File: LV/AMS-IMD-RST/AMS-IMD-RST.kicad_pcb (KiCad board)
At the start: 2 copper layers, 66.8 x 64.2 mm, 38 parts, among them J1 2P Droit 2-11-2022, J2 2P Droit 2-11-2022, J3 2P Droit 2-11-2022, J4 2P Droit 2-11-2022, J5 2P Droit 2-11-2022, J6 2P Droit 2-11-2022, J7 4P Droit 22-11-2042, K1 Relais PCB, K3 Relais PCB, Q5 NMOS SQ2348ES-T1_GE3, Q6 NMOS SQ2348ES-T1_GE3, U1 Alim LP TSR_0.5-2450, U10 TLV172IDCK, U11 74AUC2G00, U14 74AHC1G08, U15 74AHC1G08, U16 74AHC1G08, U17 TLV172IDCK, U2 MCP6562, U3 74AHC1G32, U4 74AUC2G04, U5 MCP6562, U6 MCP6562, U7 74LS279, U9 TLV172IDCK

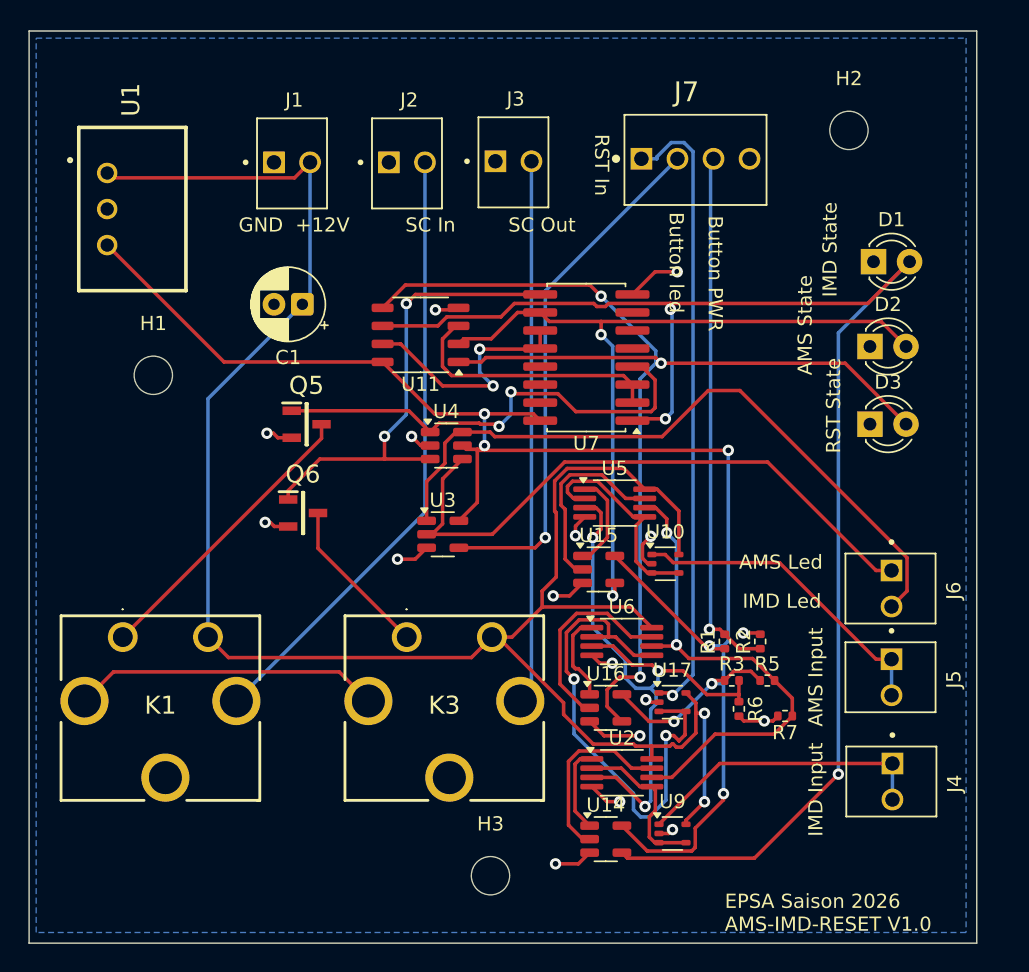
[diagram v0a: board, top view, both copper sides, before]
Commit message: Added 2s lightning for T11.9.6 compliance
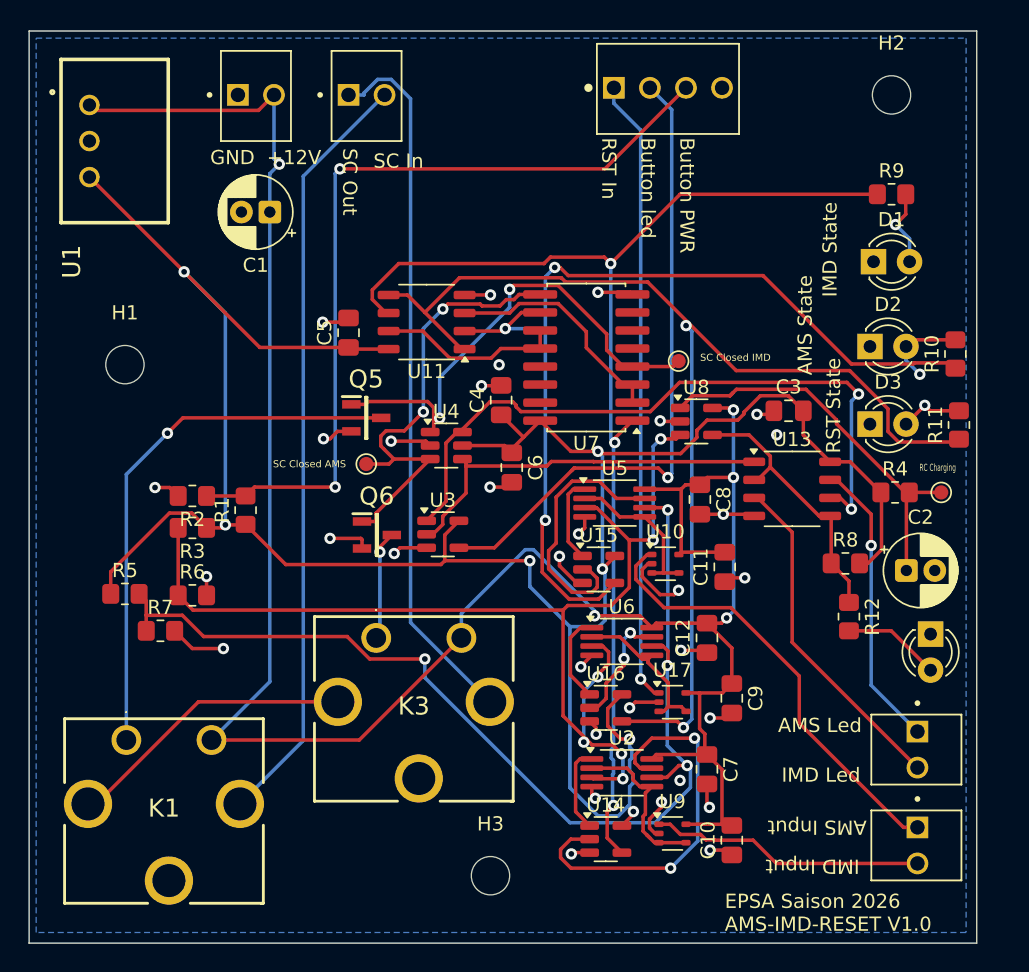
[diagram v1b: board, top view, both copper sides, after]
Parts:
- removed J3, J5: 2P Droit 2-11-2022, EPSA_lib:MOLEX_22-11-2022
- added C10: 100n, Capacitor_SMD:C_0805_2012Metric_Pad1.18x1.45mm_HandSolder, F.Cu at (117.8, 92.8)
- added C11: 100n, Capacitor_SMD:C_0805_2012Metric_Pad1.18x1.45mm_HandSolder, F.Cu at (117.2, 73.5)
- added C12: 100n, Capacitor_SMD:C_0805_2012Metric_Pad1.18x1.45mm_HandSolder, F.Cu at (116.0, 78.5)
- added C2: 10u, Capacitor_THT:CP_Radial_D5.0mm_P2.00mm, F.Cu at (130.0, 73.8)
- added C3: 100n, Capacitor_SMD:C_0805_2012Metric_Pad1.18x1.45mm_HandSolder, F.Cu at (121.8, 62.5)
- added C4: 100n, Capacitor_SMD:C_0805_2012Metric_Pad1.18x1.45mm_HandSolder, F.Cu at (101.5, 61.8)
- added C5: 100n, Capacitor_SMD:C_0805_2012Metric_Pad1.18x1.45mm_HandSolder, F.Cu at (90.8, 57.0)
- added C6: 100n, Capacitor_SMD:C_0805_2012Metric_Pad1.18x1.45mm_HandSolder, F.Cu at (102.2, 66.5)
- added C7: 100n, Capacitor_SMD:C_0805_2012Metric_Pad1.18x1.45mm_HandSolder, F.Cu at (116.0, 87.8)
- added C8: 100n, Capacitor_SMD:C_0805_2012Metric_Pad1.18x1.45mm_HandSolder, F.Cu at (115.5, 68.8)
- added C9: 100n, Capacitor_SMD:C_0805_2012Metric_Pad1.18x1.45mm_HandSolder, F.Cu at (117.8, 82.8)
- added D4: LED, LED_THT:LED_D3.0mm, F.Cu at (131.8, 78.2)
- added R10: 10k, Resistor_SMD:R_0805_2012Metric_Pad1.20x1.40mm_HandSolder, F.Cu at (133.5, 58.5)
- added R11: 10k, Resistor_SMD:R_0805_2012Metric_Pad1.20x1.40mm_HandSolder, F.Cu at (133.8, 63.5)
- added R12: 10k, Resistor_SMD:R_0805_2012Metric_Pad1.20x1.40mm_HandSolder, F.Cu at (126.0, 77.0)
- added R4: 62k, Resistor_SMD:R_0805_2012Metric_Pad1.20x1.40mm_HandSolder, F.Cu at (129.2, 68.2)
- added R8: 10k, Resistor_SMD:R_0805_2012Metric_Pad1.20x1.40mm_HandSolder, F.Cu at (125.8, 73.2)
- added R9: 10k, Resistor_SMD:R_0805_2012Metric_Pad1.20x1.40mm_HandSolder, F.Cu at (129.0, 47.2)
- added TP1: type="R" model="TestPoint" lib="", TestPoint:TestPoint_Pad_D1.0mm, F.Cu at (92.0, 66.2)
- added TP2: type="R" model="TestPoint" lib="", TestPoint:TestPoint_Pad_D1.0mm, F.Cu at (114.0, 59.0)
- added TP3: type="R" model="TestPoint" lib="", TestPoint:TestPoint_Pad_D1.0mm, F.Cu at (132.5, 68.2)
- added U13: 74AUC2G32, Package_SO:SSOP-8_3.9x5.05mm_P1.27mm, F.Cu at (122.0, 68.0)
- added U8: LM397, Package_TO_SOT_SMD:SOT-23-5, F.Cu at (115.2, 63.2)
- R1, R2, R3, R5, R6, R7: footprint Resistor_SMD:R_0402_1005Metric -> Resistor_SMD:R_0805_2012Metric_Pad1.20x1.40mm_HandSolder
- moved R5 45.7 mm to (75.0, 75.4)
- moved R7 44.4 mm to (77.5, 78.0), turned to 0 degrees
- moved R2 41.3 mm to (79.8, 68.5), turned to 180 degrees
- moved R3 39.5 mm to (79.8, 70.8), turned to 180 degrees
- moved R6 39.3 mm to (79.8, 75.5), turned to 0 degrees
- moved R1 35.0 mm to (83.5, 69.5)
- moved J6 11.5 mm to (130.8, 85.1)
- moved K1 7.25 mm to (75.1, 85.7)
- moved C1 6.89 mm to (85.2, 48.5)
- moved J2 5.54 mm to (90.8, 40.2)
- moved Q6 5.43 mm to (92.8, 71.2)
- moved J1 5.39 mm to (83.0, 40.2)
- moved J7 5.36 mm to (113.2, 39.8)
- moved U1 4.95 mm to (70.5, 37.8)
- moved J4 4.83 mm to (130.8, 91.8)
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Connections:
- D1 pad 2: /IMD_State -> Net-(D1-A)
- D2 pad 2: /AMS_State -> Net-(D2-A)
- D3 pad 2: /Button_Output_State -> Net-(D3-A)
- J2 pad 1: GND -> /SC out
- J4 pad 1: /Raw_IMD_OK -> /Raw_AMS_OK
- U3 pad 1: /IMD_Led -> /Raw_IMD_Led
- U3 pad 2: /AMS_Led -> /Raw_AMS_Led
- U4 pad 4: /AMS_Led -> /Raw_AMS_Led
- U4 pad 6: /IMD_Led -> /Raw_IMD_Led
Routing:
- net +5V: track 122.4 -> 178.7 mm
- net /Raw_IMD_Led: track 0.00 -> 48.1 mm, vias 0 -> 2
- net /3.5V: track 35.5 -> 76.1 mm, vias 2 -> 4
- net /4V: track 44.3 -> 81.0 mm, vias 3 -> 6
- net Net-(U8--): track 0.00 -> 27.9 mm
- net /Raw_AMS_Led: track 0.00 -> 27.3 mm
- net Net-(U17--): track 36.4 -> 11.1 mm, vias 2 -> 0
- net /IMD_Led: track 49.1 -> 23.9 mm
- net /AMS_Led: track 44.4 -> 20.6 mm, vias 0 -> 1
- net GND: track 36.8 -> 60.5 mm, vias 17 -> 32
- net +12V: track 139.6 -> 163.1 mm, vias 2 -> 5
- net /Button_Input_SCS: track 37.4 -> 58.6 mm, vias 1 -> 2
- net /IMD_State: track 105.9 -> 85.5 mm
- net /initLed: track 0.00 -> 19.3 mm
- net Net-(K1-Pad1): track 20.8 -> 38.3 mm, vias 0 -> 1
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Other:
- board text added: "RC Charging"
- board text added: "SC Closed AMS"
- board text added: "SC Closed IMD"

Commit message: Added test LEDS and testpoints on schem
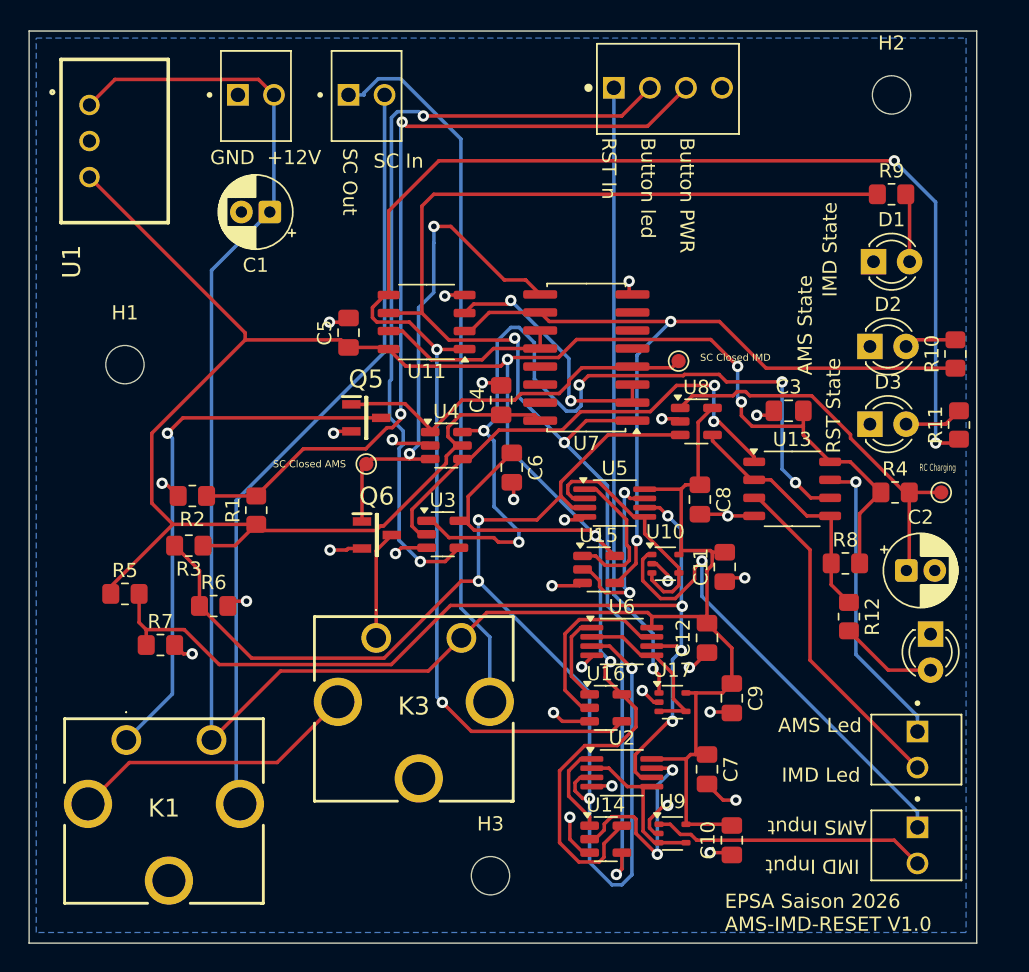
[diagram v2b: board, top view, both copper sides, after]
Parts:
- moved R6 1.68 mm to (81.2, 76.2)
- moved R3 1.27 mm to (79.5, 72.0)
- moved R7 1.00 mm to (77.5, 79.0)
- moved R1 0.75 mm to (84.2, 69.5)
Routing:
- net /Button_Output_State: track 84.9 -> 114.3 mm, vias 2 -> 4
- net +5V: track 178.7 -> 201.6 mm, vias 7 -> 5
- net /4V: track 81.0 -> 100.1 mm, vias 6 -> 4
- net +12V: track 163.1 -> 148.5 mm, vias 5 -> 0
- net /Raw_IMD_Led: track 48.1 -> 61.4 mm, vias 2 -> 5
- net /IMD_State: track 85.5 -> 97.9 mm
- net Net-(U14-Pad2): track 27.6 -> 15.3 mm
- net /AMS_State: track 68.1 -> 56.9 mm, vias 3 -> 2
- net /LED_Button: track 45.8 -> 54.9 mm, vias 1 -> 2
- net /SC_Closed_IMD: track 34.6 -> 27.3 mm, vias 2 -> 0
- net /Raw_AMS_Led: track 27.3 -> 34.2 mm, vias 0 -> 2
- net /3.5V: track 76.1 -> 69.7 mm
- net GND: track 60.5 -> 54.2 mm, vias 32 -> 29
- net Net-(U10--): track 11.2 -> 17.2 mm
- net Net-(U15-Pad2): track 18.7 -> 13.0 mm, vias 0 -> 2
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
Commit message: PCB rooting finished
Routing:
- net GND: track 54.2 -> 63.9 mm
- net /LED_Button: track 54.9 -> 59.2 mm
- net /Raw_IMD_Led: track 61.4 -> 64.4 mm
- net /4V: track 100.1 -> 102.4 mm

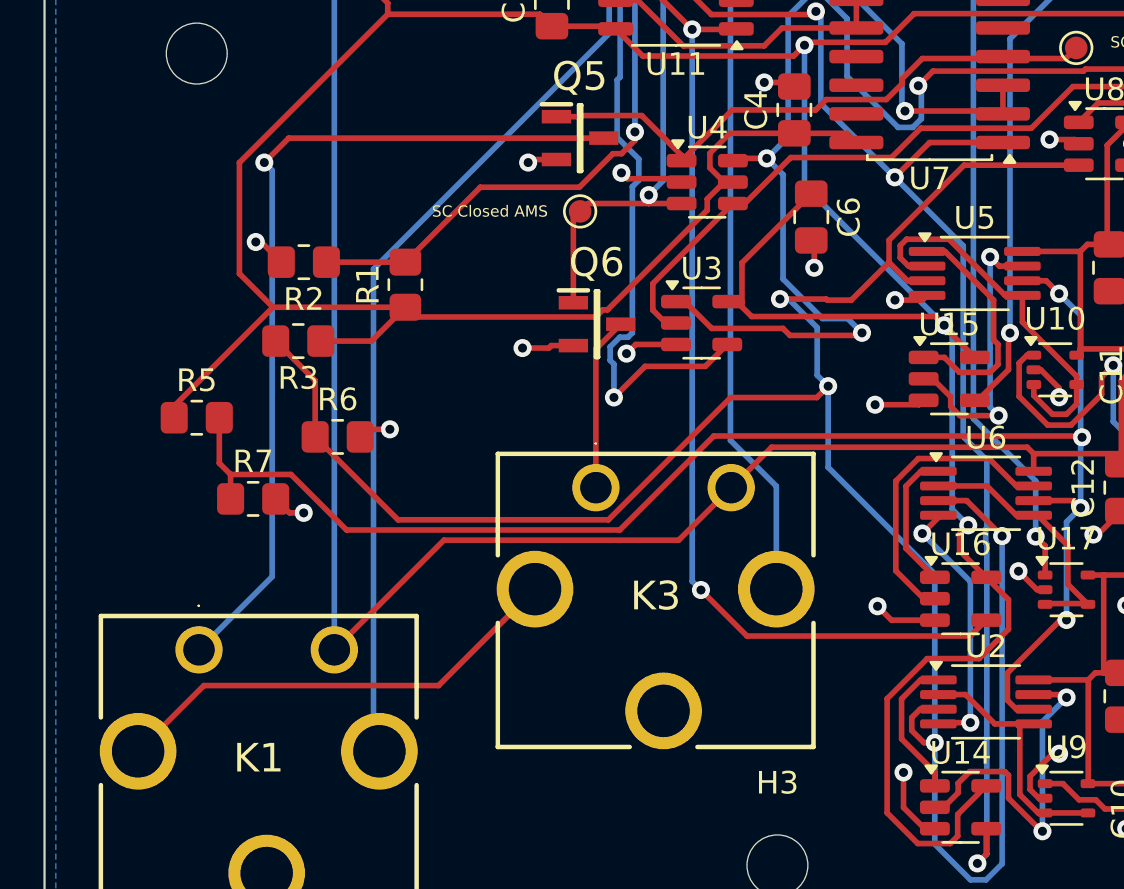
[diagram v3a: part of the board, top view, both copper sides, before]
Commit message: Résolution problème AMS IMD RST
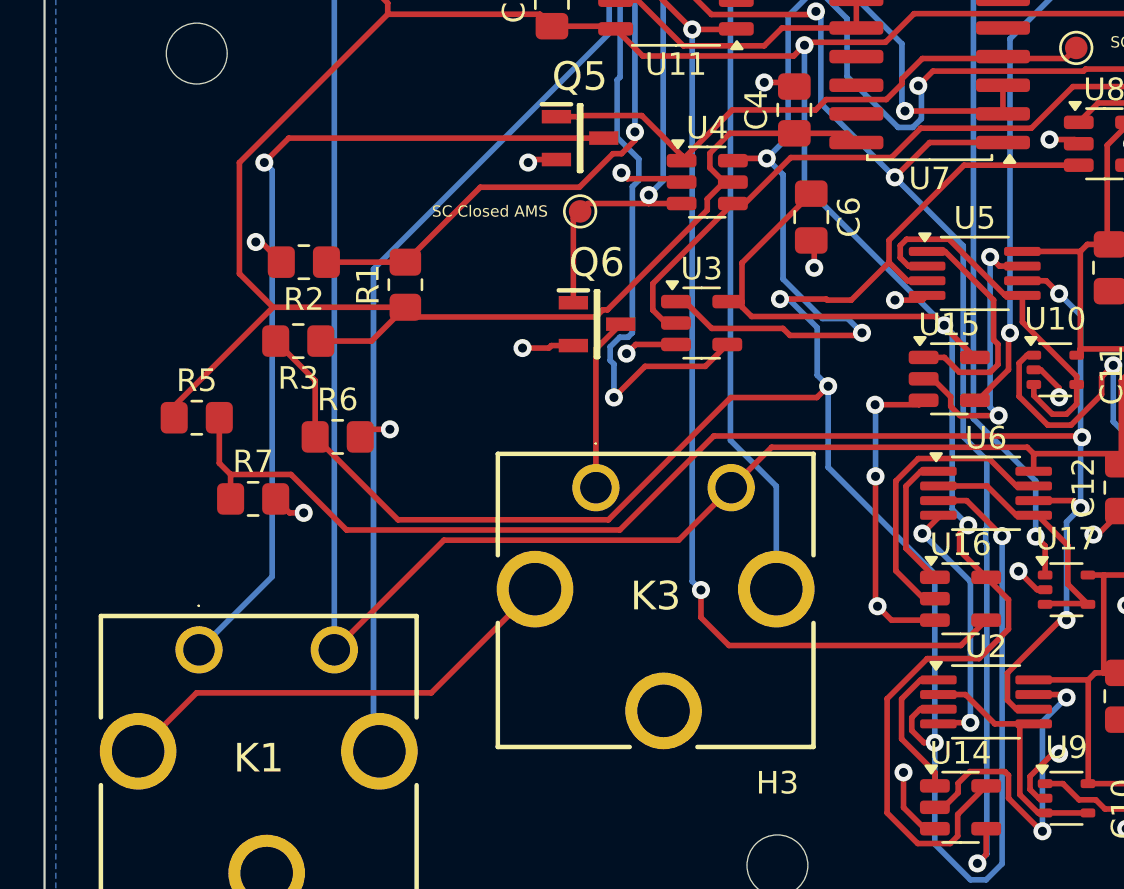
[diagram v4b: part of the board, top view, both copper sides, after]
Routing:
- net GND: track 63.9 -> 72.8 mm, vias 29 -> 30
- net /Button_Output_State: track 114.3 -> 115.4 mm
